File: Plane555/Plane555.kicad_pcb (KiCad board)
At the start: 2 copper layers, 106.6 x 90.2 mm, 32 parts, among them SW1 SW_SPDT

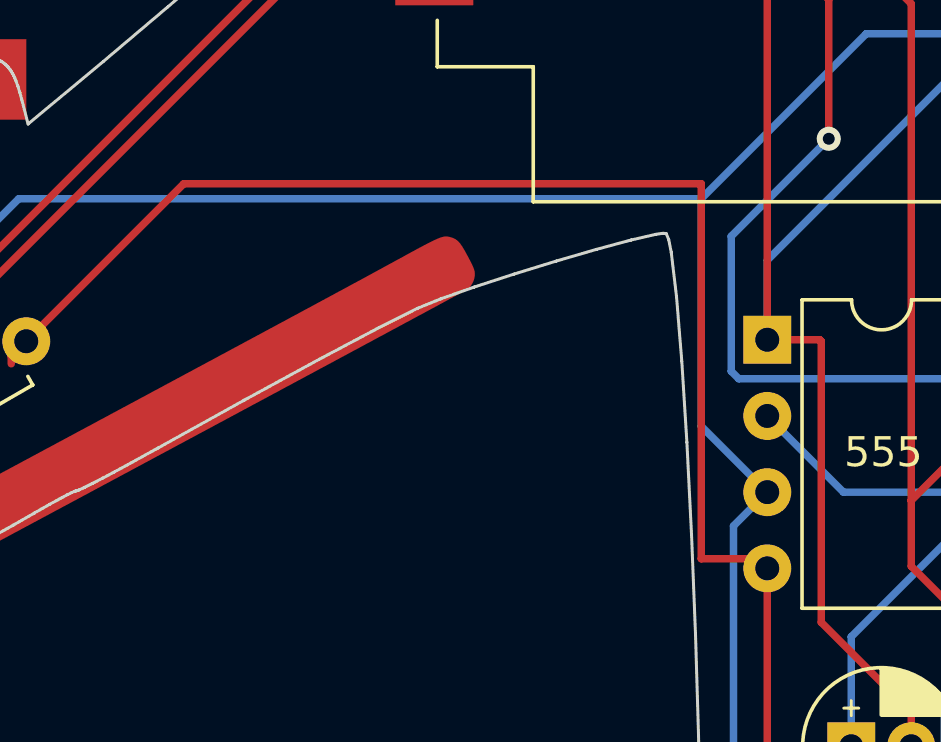
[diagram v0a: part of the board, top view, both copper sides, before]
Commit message: feat: update board trace and R values
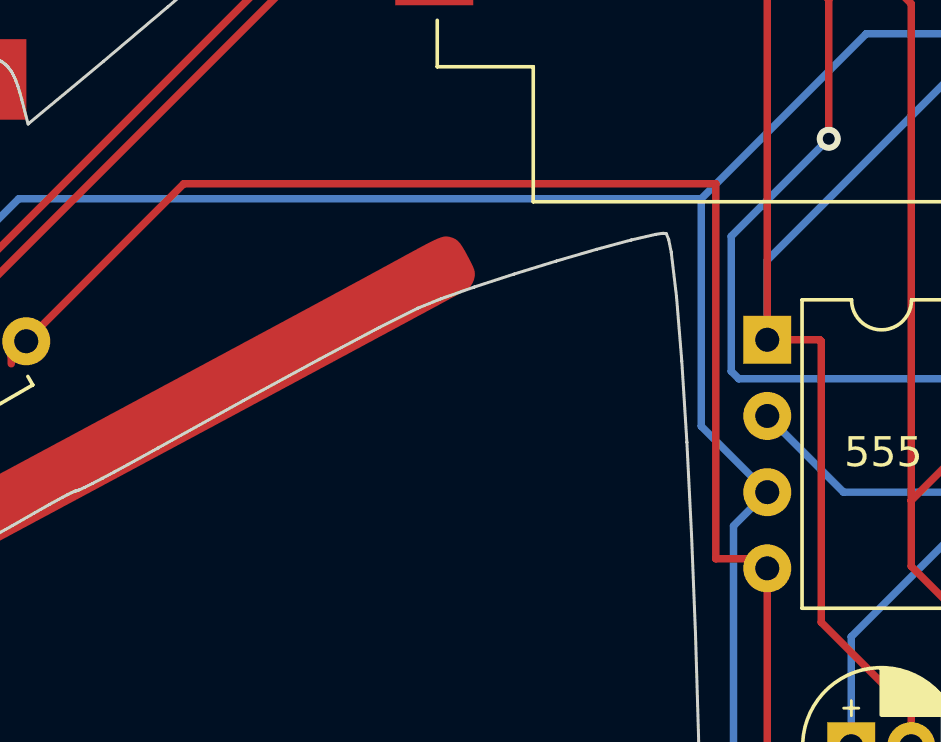
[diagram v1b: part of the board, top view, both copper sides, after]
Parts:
- R1: value 100k ohm -> 10k ohm
- R2: value 100k ohm -> 220 ohm
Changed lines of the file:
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@@
         (effects (font (size 1 1) (thickness 0.15)))
     )
-    (fp_text value "100k ohm" (at 3.81 2.37 -30) (layer "F.Fab")
+    (fp_text value "220 ohm" (at 3.81 2.37 -30) (layer "F.Fab")
         (effects (font (size 1 1) (thickness 0.15)))
     )
@@
         (effects (font (size 1 1) (thickness 0.15)))
     )
-    (fp_text value "100k ohm" (at 3.81 2.37 30) (layer "F.Fab")
+    (fp_text value "10k ohm" (at 3.81 2.37 30) (layer "F.Fab")
         (effects (font (size 1 1) (thickness 0.15)))
     )
@@
   (segment (start 141 58.5) (end 139.5 60) (width 0.25) (layer "F.Cu") (net 2))
   (segment (start 143.25 58.5) (end 141 58.5) (width 0.25) (layer "F.Cu") (net 2))
+  (segment (start 135.38 94) (end 135.7 94.32) (width 0.25) (layer "F.Cu") (net 3))
+  (segment (start 133.985 81.5) (end 133.985 94) (width 0.25) (layer "F.Cu") (net 3))
   (segment (start 143.32 61.28) (end 142.04 60) (width 0.25) (layer "F.Cu") (net 3))
   (segment (start 143.75 113.25) (end 143.75 96) (width 0.25) (layer "F.Cu") (net 3))
   (segment (start 144.75 88.13) (end 143.32 86.7) (width 0.25) (layer "F.Cu") (net 3))
-  (segment (start 110.5 87.250001) (end 116.250001 81.5) (width 0.25) (layer "F.Cu") (net 3))
   (segment (start 144.75 95) (end 144.75 88.13) (width 0.25) (layer "F.Cu") (net 3))
   (segment (start 139.5 116.5) (end 140.5 116.5) (width 0.25) (layer "F.Cu") (net 3))
@@
   (segment (start 135.7 94.32) (end 135.7 112.7) (width 0.25) (layer "F.Cu") (net 3))
   (segment (start 140.5 116.5) (end 143.75 113.25) (width 0.25) (layer "F.Cu") (net 3))
-  (segment (start 110.5 87.5) (end 110.5 87.250001) (width 0.25) (layer "F.Cu") (net 3))
+  (segment (start 110.5 87.250001) (end 116.250001 81.5) (width 0.25) (layer "F.Cu") (net 3))
   (segment (start 143.75 96) (end 144.75 95) (width 0.25) (layer "F.Cu") (net 3))
+  (segment (start 133.985 94) (end 135.38 94) (width 0.25) (layer "F.Cu") (net 3))
   (segment (start 135.7 112.7) (end 139.5 116.5) (width 0.25) (layer "F.Cu") (net 3))
-  (segment (start 133.5 81.5) (end 133.5 94) (width 0.25) (layer "F.Cu") (net 3))
-  (segment (start 135.38 94) (end 135.7 94.32) (width 0.25) (layer "F.Cu") (net 3))
-  (segment (start 133.5 94) (end 135.38 94) (width 0.25) (layer "F.Cu") (net 3))
-  (segment (start 116.250001 81.5) (end 133.5 81.5) (width 0.25) (layer "F.Cu") (net 3))
+  (segment (start 116.250001 81.5) (end 133.985 81.5) (width 0.25) (layer "F.Cu") (net 3))
+  (segment (start 110.5 87.5) (end 110.5 87.250001) (width 0.25) (layer "F.Cu") (net 3))
   (segment (start 140.5 92.06) (end 143.32 89.24) (width 0.25) (layer "F.Cu") (net 4))
   (segment (start 133.25 68.25) (end 125.5 68.25) (width 0.25) (layer "F.Cu") (net 4))

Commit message: feat: update R values
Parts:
- R1: value 10k ohm -> 1.2k ohm
- R2: value 220 ohm -> 90 ohm
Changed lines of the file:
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@@
         (effects (font (size 1 1) (thickness 0.15)))
     )
-    (fp_text value "220 ohm" (at 3.81 2.37 -30) (layer "F.Fab")
+    (fp_text value "90 ohm" (at 3.81 2.37 -30) (layer "F.Fab")
         (effects (font (size 1 1) (thickness 0.15)))
     )
@@
         (effects (font (size 1 1) (thickness 0.15)))
     )
-    (fp_text value "10k ohm" (at 3.81 2.37 30) (layer "F.Fab")
-        (effects (font (size 1 1) (thickness 0.15)))
-    )
+    (fp_text value "1.2k ohm" (at 3.81 2.37 30) (layer "F.Fab")
+        (effects (font (size 1 1) (thickness 0.15)))
+    )

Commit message: feat: update silk screen
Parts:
- C1: value C -> 10uf
- RV1: value POT -> 100k POT
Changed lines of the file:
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@@
       (outputformat 1)
       (mirror false)
-      (drillshape 1)
+      (drillshape 0)
       (scaleselection 1)
       (outputdirectory "")
@@
         (effects (font (size 1 1) (thickness 0.15)))
     )
-    (fp_text value "POT" (at -2.5 -2.58) (layer "F.SilkS")
+    (fp_text value "100k POT" (at -2.5 -2.58) (layer "F.SilkS")
         (effects (font (size 1 1) (thickness 0.15)))
     )
@@
         (effects (font (size 1 1) (thickness 0.15)))
     )
-    (fp_text value "90 ohm" (at 3.81 2.37 -30) (layer "F.Fab")
+    (fp_text value "90 ohm" (at 3.81 2.37 -30) (layer "F.SilkS")
         (effects (font (size 1 1) (thickness 0.15)))
     )
@@
         (effects (font (size 1 1) (thickness 0.15)))
     )
-    (fp_text value "1.2k ohm" (at 3.81 2.37 30) (layer "F.Fab")
+    (fp_text value "1.2k ohm" (at 3.81 2.37 30) (layer "F.SilkS")
         (effects (font (size 1 1) (thickness 0.15)))
     )
@@
         (effects (font (size 1 1) (thickness 0.15)))
     )
-    (fp_text value "C" (at 1 3.75) (layer "F.Fab")
-        (effects (font (size 1 1) (thickness 0.15)))
-    )
+    (fp_text value "10uf " (at 1 3.75) (layer "F.SilkS")
+        (effects (font (size 1 1) (thickness 0.15)))
+    )

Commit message: feat: init new files
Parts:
- removed the G*** at (121.5, 67.0) (x2)
- removed the G*** at (170.2, 78.2) (x2)
- removed the G*** at (149.2, 123.2) (x2)
- removed the G*** at (139.2, 43.2) (x2)
- removed the G*** at (132.0, 121.6) (x2)
- removed the G*** at (108.5, 78.0) (x2)
- removed the G*** at (165.2, 90.2) (x2)
- removed the G*** at (139.0, 122.0) (x2)
- removed the G*** at (112.1, 90.9) (x2)
- removed the G*** at (139.5, 84.5)
- removed the G*** at (157.2, 66.8) (x2)
- removed RV1: 100k POT, Potentiometer_THT:Potentiometer_Bourns_3386P_Vertical
- added 100k POT: POT, Potentiometer_THT:Potentiometer_Bourns_3386P_Vertical, F.Cu at (123.0, 126.5)
- added G*** (x2): LOGO, LOGO, F.Cu at (136.4, 140.2)
- added G*** (x2): LOGO, LOGO, F.Cu at (155.8, 105.2)
- added G***: LOGO, LOGO, B.Cu at (125.7, 97.5)
- added G*** (x2): LOGO, LOGO, F.Cu at (116.6, 138.9)
- added G*** (x2): LOGO, LOGO, F.Cu at (125.5, 53.1)
- added G*** (x2): LOGO, LOGO, F.Cu at (93.4, 106.4)
- C1: value 10uf -> 10uf
- D1: footprint LED_THT:LED_D3.0mm -> LED_THT:LED_D3.0mm_Horizontal_O1.27mm_Z2.0mm; moved to B.Cu
- D3: footprint LED_THT:LED_D3.0mm_Horizontal_O1.27mm_Z2.0mm -> LED_THT:LED_D3.0mm; moved to F.Cu
- SW1: footprint SW SS12D:Schiebeschalter SS-12D00.kicad_mod -> Button_Switch_THT:Schiebeschalter_SS-12D00
- moved D2 114.8 mm to (71.6, 115.6)
- moved D1 51.1 mm to (126.8, 135.7), turned to 180 degrees
- moved D3 35.5 mm to (175.8, 114.5), turned to 0 degrees
- moved C1 21.6 mm to (124.4, 116.6)
- moved 555 19.9 mm to (121.6, 100.8)
- moved R1 19.9 mm to (89.4, 103.6)
- moved ? 19.3 mm to (146.8, 91.6), turned to 0 degrees
- moved BATTERY 18.6 mm to (125.3, 86.0), turned to 0 degrees
- moved R2 18.0 mm to (155.5, 99.9)
- moved SW1 16.5 mm to (125.6, 68.8)
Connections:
- R1 pad 1: Net-(U1-DIS) -> GNDREF
- R1 pad 2: +3V0 -> Net-(D1-K)
- R2 pad 1: GNDREF -> Net-(U1-DIS)
- R2 pad 2: Net-(D1-K) -> +3V0
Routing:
- net +3V0: track 124.6 -> 82.9 mm
- net Net-(D1-A): track 152.1 -> 186.6 mm
- net Net-(U1-DIS): track 92.6 -> 65.7 mm
- net GNDREF: track 75.1 -> 86.0 mm, vias 0 -> 1
- net Net-(U1-THR): track 29.5 -> 33.4 mm
- net Net-(D1-K): track 202.9 -> 205.4 mm, vias 1 -> 0
- net Net-(BT1-+): track 24.0 -> 23.4 mm
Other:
- board size 106.6 x 90.2 mm -> 115.1 x 97.3 mm
